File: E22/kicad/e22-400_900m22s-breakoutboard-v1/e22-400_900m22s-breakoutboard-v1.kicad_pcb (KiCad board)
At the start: 2 copper layers, 30 x 27 mm, 13 parts, among them IC1 E22-900M22S, J1 Conn_01x06_Pin, J2 Conn_01x06_Pin, SW1 LORA_RESET, U1 AMS1117-3.3

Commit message: Layout and routing
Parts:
- C1, C2, C3, C4: footprint Capacitor_SMD:C_0805_2012Metric_Pad1.18x1.45mm_HandSolder -> Capacitor_SMD:C_0603_1608Metric_Pad1.08x0.95mm_HandSolder
- D1: footprint LED_SMD:LED_0805_2012Metric_Pad1.15x1.40mm_HandSolder -> LED_SMD:LED_0603_1608Metric_Pad1.05x0.95mm_HandSolder
- J1, J2: value Conn_01x06_Pin -> Conn_01x08_Pin; footprint Connector_PinHeader_2.54mm:PinHeader_1x06_P2.54mm_Vertical -> Connector_PinHeader_2.54mm:PinHeader_1x08_P2.54mm_Vertical
- R1: footprint Resistor_SMD:R_0805_2012Metric_Pad1.20x1.40mm_HandSolder -> Resistor_SMD:R_0603_1608Metric_Pad0.98x0.95mm_HandSolder
- moved JP1 3.04 mm to (132.2, 116.8), turned to 180 degrees
- moved J1 1.86 mm to (153.9, 120.0)
- moved J2 1.86 mm to (153.9, 93.0)
- moved C1 0.45 mm to (136.5, 112.9)
- moved D1 0.45 mm to (131.5, 112.9)
- moved R1 0.45 mm to (134.0, 112.9)
- moved C4 0.41 mm to (157.5, 116.2), turned to 0 degrees
- moved C2 0.25 mm to (132.5, 96.9)
- moved C3 0.25 mm to (136.0, 108.5)
- moved U1 0.25 mm to (134.0, 102.8)
- moved SW1 0.10 mm to (157.5, 110.0)
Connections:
- H1 pad 1: (no net) -> /ANT
- IC1 pad 21: Net-(IC1-ANT) -> /ANT
- J1 pad 5: /SCK -> GND
- J1 pad 6: /NSS -> /SCK
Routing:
- net VCC: track 0.00 -> 49.0 mm, vias 0 -> 2
- net /NRST: track 0.00 -> 46.8 mm
- net GND: track 0.00 -> 45.7 mm, vias 0 -> 23
- net /DIO1: track 0.00 -> 29.9 mm
- net /DIO2: track 0.00 -> 25.2 mm
- net /TXEN: track 0.00 -> 25.1 mm, vias 0 -> 2
- net /BUSY: track 0.00 -> 24.6 mm, vias 0 -> 2
- net /NSS: track 0.00 -> 24.6 mm, vias 0 -> 1
- net /RXEN: track 0.00 -> 23.2 mm, vias 0 -> 2
- net /SCK: track 0.00 -> 20.2 mm, vias 0 -> 1
- net +3V3: track 0.00 -> 17.4 mm
- net /MOSI: track 0.00 -> 16.5 mm, vias 0 -> 1
- net /MISO: track 0.00 -> 13.8 mm, vias 0 -> 1
- net /ANT: track 0.00 -> 4.01 mm
- net Net-(D1-A): track 0.00 -> 2.52 mm
- added copper zone on F.Cu, net +3V3
- added copper zone on B.Cu, net GND
- added copper zone on F.Cu, net GND
- added copper zone on F.Cu, net VCC
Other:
- board text added: "BUSY"
- board text added: "DIO1"
- board text added: "DIO2"
- board text added: "GND"
- board text added: "MISO"
- board text added: "MOSI"
- board text added: "NRST"
- board text added: "NSS"
- board text added: "RXEN"
- board text added: "SCK"
- board text added: "TXEN"
- board text added: "VCC"
- board text added: "eByte LoRa Breakout Board E22-400/900M22S Rev. 1.0 04/24 By Gabriel Vega"
- board text added: "todo: confirm pin spacing for breadboard confirm hole size for antenna confirm keepout zone for antenna confirm push-buttom footprint"
- board text removed: "todo: confirm pin spacing for breadboard confirm hole size for antenna"

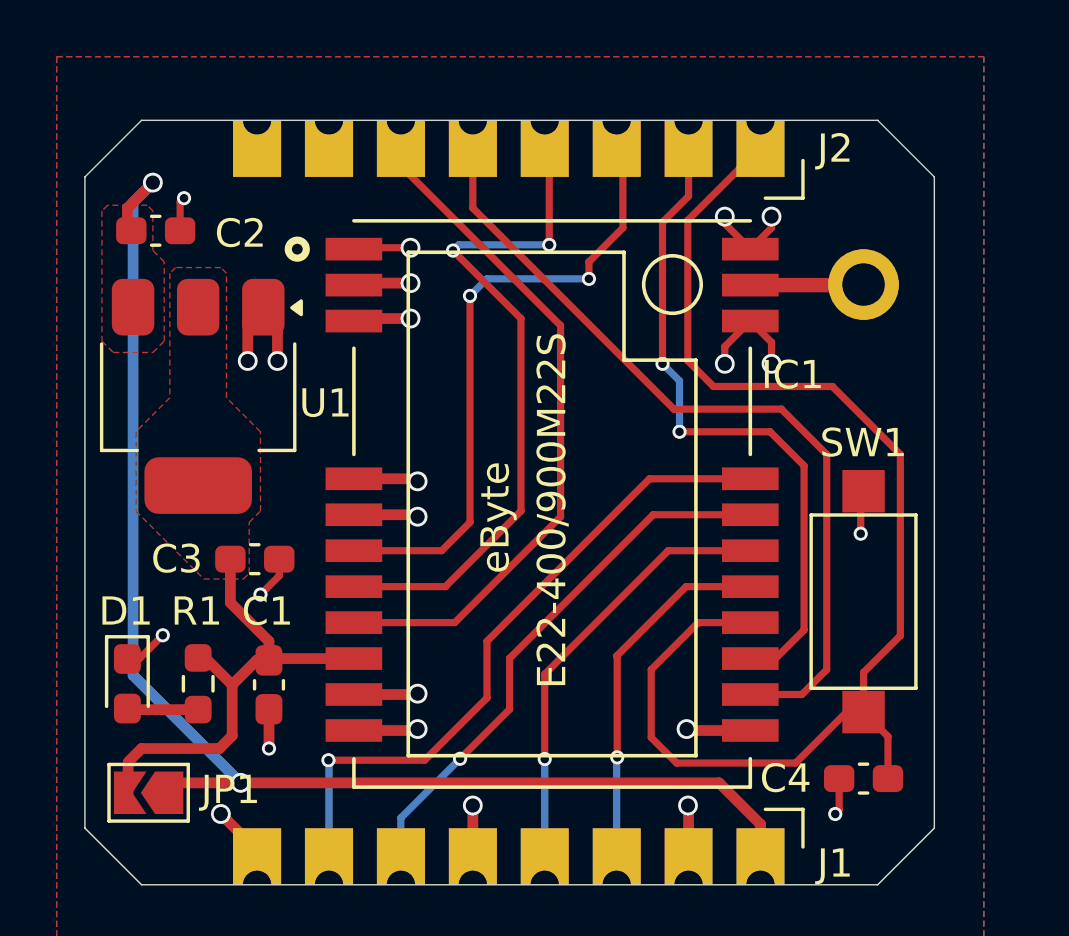
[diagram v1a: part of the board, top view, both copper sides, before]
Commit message: Add led for busy pin. Layout Adjusted
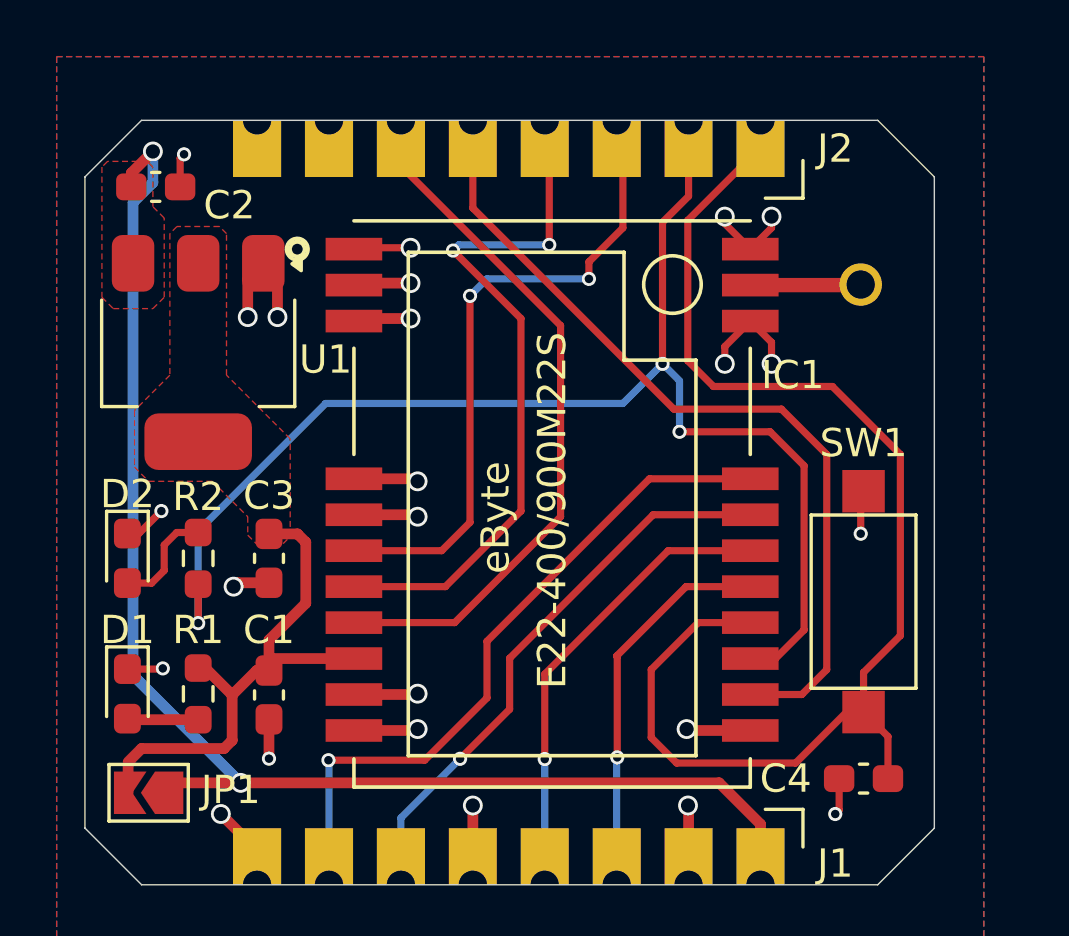
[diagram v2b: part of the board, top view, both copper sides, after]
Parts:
- added D2: LED_BUSY, LED_SMD:LED_0603_1608Metric_Pad1.05x0.95mm_HandSolder, F.Cu at (131.5, 108.5)
- added R2: 1K, Resistor_SMD:R_0603_1608Metric_Pad0.98x0.95mm_HandSolder, F.Cu at (134.0, 108.5)
- moved C2 1.55 mm to (132.5, 95.3)
- moved U1 1.55 mm to (134.0, 101.2)
- moved C3 0.50 mm to (136.5, 108.5), turned to -90 degrees
- moved C1 0.36 mm to (136.5, 113.3)
- moved D1 0.36 mm to (131.5, 113.3)
- moved R1 0.36 mm to (134.0, 113.3)
- moved H1 0.10 mm to (157.4, 98.8)
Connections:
- H1 pad 1: /ANT -> (no net)
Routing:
- net /BUSY: track 24.6 -> 48.3 mm, vias 2 -> 3
- net Net-(D2-A): track 0.00 -> 3.77 mm
- net +3V3: track 17.4 -> 19.5 mm
- net GND: track 45.7 -> 46.6 mm, vias 23 -> 24
- net VCC: track 49.0 -> 49.5 mm

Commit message: Updated title block. Pcb finished
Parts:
- moved H1 1.15 mm to (156.2, 98.8)
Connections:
- H1 pad 1: (no net) -> /ANT
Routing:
- net /ANT: track 4.01 -> 2.76 mm
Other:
- board size 30 x 27 mm -> 30 x 27.5 mm
- board text added: "RESET"
- board text removed: "todo: confirm pin spacing for breadboard confirm hole size for antenna confirm keepout zone for antenna confirm push-buttom footprint"
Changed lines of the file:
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@@
 		(company "Libertalia Engineering")
 		(comment 1 "eByte Breakoutboards")
-		(comment 2 "Under Development")
+		(comment 2 "Finished")
 		(comment 3 "Gabriel Vega")
 		(comment 4 "Gabriel Vega")
@@
 			)
 		)
-		(sheetname "Root")
-		(sheetfile "e22-400_900m22s-breakoutboard-v1.kicad_sch")
 		(attr smd)
 		(fp_line
@@
 		)
 		(fp_circle
-			(center 9 9)
-			(end 9.381 9)
+			(center 8.75 9.75)
+			(end 9.131 9.75)
 			(stroke
 				(width 0.127)
@@
 		)
 		(fp_circle
-			(center 9 9)
-			(end 9.254 9)
+			(center 8.75 9.75)
+			(end 9.004 9.75)
 			(stroke
 				(width 0.127)
@@
 		(tags "SPST button tactile switch")
 		(property "Reference" "SW1"
-			(at 5.6 0 0)
+			(at 0.25 0 0)
 			(layer "F.SilkS")
 			(effects
@@
 	(footprint "MountingHole:MountingHole_2.2mm_M2_DIN965_Pad"
 		(layer "F.Cu")
-		(at 157.4 98.8)
+		(at 156.25 98.8)
 		(descr "Mounting Hole 2.2mm, M2, DIN965")
 		(tags "mounting hole 2.2mm m2 din965")
@@
 			(layers "*.Cu" "*.Mask")
 			(remove_unused_layers no)
+			(net 15 "/ANT")
 		)
 	)
@@
 		)
 		(property "Value" "1K"
-			(at 0 1.43 270)
+			(at 0 1.43 -90)
 			(layer "F.Fab")
 			(effects
@@
 		)
 		(fp_text user "${REFERENCE}"
-			(at 0 0 270)
+			(at 0 0 -90)
 			(layer "F.Fab")
 			(effects
@@
 	)
 	(gr_line
-		(start 158 120)
-		(end 160 118)
+		(start 158 120.25)
+		(end 160 118.25)
 		(stroke
 			(width 0.05)
@@
 	)
 	(gr_line
-		(start 160 118)
-		(end 160 95)
+		(start 160 118.25)
+		(end 160 94.75)
 		(stroke
 			(width 0.05)
@@
 	)
 	(gr_line
-		(start 132 120)
-		(end 130 118)
+		(start 132 120.25)
+		(end 130 118.25)
 		(stroke
 			(width 0.05)
@@
 	)
 	(gr_line
-		(start 158 93)
-		(end 132 93)
+		(start 158 92.75)
+		(end 132 92.75)
 		(stroke
 			(width 0.05)
@@
 	)
 	(gr_line
-		(start 160 95)
-		(end 158 93)
+		(start 160 94.75)
+		(end 158 92.75)
 		(stroke
 			(width 0.05)
@@
 	)
 	(gr_line
-		(start 132 120)
-		(end 158 120)
+		(start 132 120.25)
+		(end 158 120.25)
 		(stroke
 			(width 0.05)
@@
 	)
 	(gr_line
-		(start 130 95)
-		(end 130 118)
+		(start 130 94.75)
+		(end 130 118.25)
 		(stroke
 			(width 0.05)
@@
 	)
 	(gr_line
-		(start 130 95)
-		(end 132 93)
+		(start 130 94.75)
+		(end 132 92.75)
 		(stroke
 			(width 0.05)
@@
 			(font
 				(size 1 1)
-				(thickness 0.1)
+				(thickness 0.15)
 			)
 			(justify right bottom mirror)
@@
 			(font
 				(size 1 1)
-				(thickness 0.1)
+				(thickness 0.15)
 			)
 			(justify bottom mirror)
@@
 	)
 	(gr_text "MISO"
-		(at 148.2 117.4 -90)
+		(at 148.2 117.4 270)
 		(layer "B.SilkS")
 		(effects
 			(font
 				(size 1 1)
-				(thickness 0.1)
+				(thickness 0.15)
 			)
 			(justify left bottom mirror)
@@
 			(font
 				(size 1 1)
-				(thickness 0.1)
+				(thickness 0.15)
 			)
 			(justify left bottom mirror)
@@
 			(font
 				(size 1 1)
-				(thickness 0.1)
+				(thickness 0.15)
 			)
 			(justify right bottom mirror)
@@
 			(font
 				(size 1 1)
-				(thickness 0.1)
+				(thickness 0.15)
 			)
 			(justify right bottom mirror)
@@
 			(font
 				(size 1 1)
-				(thickness 0.1)
+				(thickness 0.15)
 			)
 			(justify left bottom mirror)
@@
 			(font
 				(size 1 1)
-				(thickness 0.1)
+				(thickness 0.15)
 			)
 			(justify right bottom mirror)
@@
 			(font
 				(size 1 1)
-				(thickness 0.1)
+				(thickness 0.15)
 			)
 			(justify left bottom mirror)
@@
 			(font
 				(size 1 1)
-				(thickness 0.1)
+				(thickness 0.15)
 			)
 			(justify left bottom mirror)
@@
 			(font
 				(size 1 1)
-				(thickness 0.1)
+				(thickness 0.15)
 			)
 			(justify right bottom mirror)
@@
 			(font
 				(size 1 1)
-				(thickness 0.1)
+				(thickness 0.15)
 			)
 			(justify right bottom mirror)
@@
 			(font
 				(size 1 1)
-				(thickness 0.1)
+				(thickness 0.15)
 			)
 			(justify right bottom mirror)
@@
 			(font
 				(size 1 1)
-				(thickness 0.1)
+				(thickness 0.15)
 			)
 			(justify left bottom mirror)
@@
 			(font
 				(size 1 1)
-				(thickness 0.1)
+				(thickness 0.15)
 			)
 			(justify left bottom mirror)
@@
 			(font
 				(size 1 1)
-				(thickness 0.1)
+				(thickness 0.15)
 			)
 			(justify right bottom mirror)
@@
 			(font
 				(size 1 1)
-				(thickness 0.1)
+				(thickness 0.15)
 			)
 			(justify left bottom mirror)
 		)
 	)
-	(gr_text "todo:\n\nconfirm pin spacing for breadboard\nconfirm hole size for antenna\nconfirm keepout zone for antenna\nconfirm push-buttom footprint"
-		(at 175 115 0)
+	(gr_text "RESET"
+		(at 155.25 104.75 0)
 		(layer "F.SilkS")
 		(effects
 			(font
 				(size 1 1)
-				(thickness 0.1)
+				(thickness 0.15)
 			)
 			(justify left bottom)
@@
 		(layer "Dwgs.User")
 		(pts
-			(xy 158 93) (xy 158 120)
+			(xy 132 93) (xy 158 93)
 		)
-		(height 13.75)
-		(orientation 1)
-		(gr_text "27 mm"
-			(at 170.6 106.5 90)
+		(height -6)
+		(orientation 0)
+		(gr_text "26 mm"
+			(at 145 85.85 0)
 			(layer "Dwgs.User")
 			(effects
@@
 		(layer "Dwgs.User")
 		(pts
-			(xy 132 93) (xy 158 93)
+			(xy 160 94.75) (xy 160 118.25)
 		)
-		(height -6)
-		(orientation 0)
-		(gr_text "26 mm"
-			(at 145 85.85 0)
+		(height 4.5)
+		(orientation 1)
+		(gr_text "23.5 mm"
+			(at 163.35 106.5 90)
 			(layer "Dwgs.User")
 			(effects
@@
 		(layer "Dwgs.User")
 		(pts
-			(xy 160 95) (xy 160 118)
+			(xy 158 92.75) (xy 158 120.25)
 		)
-		(height 6.25)
+		(height 8.75)
 		(orientation 1)
-		(gr_text "23 mm"
-			(at 165.1 106.5 90)
+		(gr_text "27.5 mm"
+			(at 165.6 106.5 90)
 			(layer "Dwgs.User")
 			(effects
@@
 	(segment
 		(start 153.5 98.82)
-		(end 157.48 98.82)
+		(end 156.23 98.82)
 		(width 0.508)
 		(layer "F.Cu")
@@
 	)
 	(segment
-		(start 157.48 98.82)
-		(end 157.5 98.8)
+		(start 156.23 98.82)
+		(end 156.25 98.8)
 		(width 0.508)
 		(layer "F.Cu")
@@
 		(polygon
 			(pts
-				(xy 160.2 101.8) (xy 155.6 101.8) (xy 154.7 100.9) (xy 154.7 96.85) (xy 155.7 95.85) (xy 160.2 95.85)
+				(xy 160.2 101.8) (xy 155.6 101.8) (xy 154.7 100.9) (xy 154.7 96.85) (xy 155.8 95.75) (xy 160.2 95.75)
 			)
 		)
